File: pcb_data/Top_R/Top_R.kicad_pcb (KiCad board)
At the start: 2 copper layers, 186.9 x 96.4 mm, 93 parts, among them U1 XIAO-nRF52840

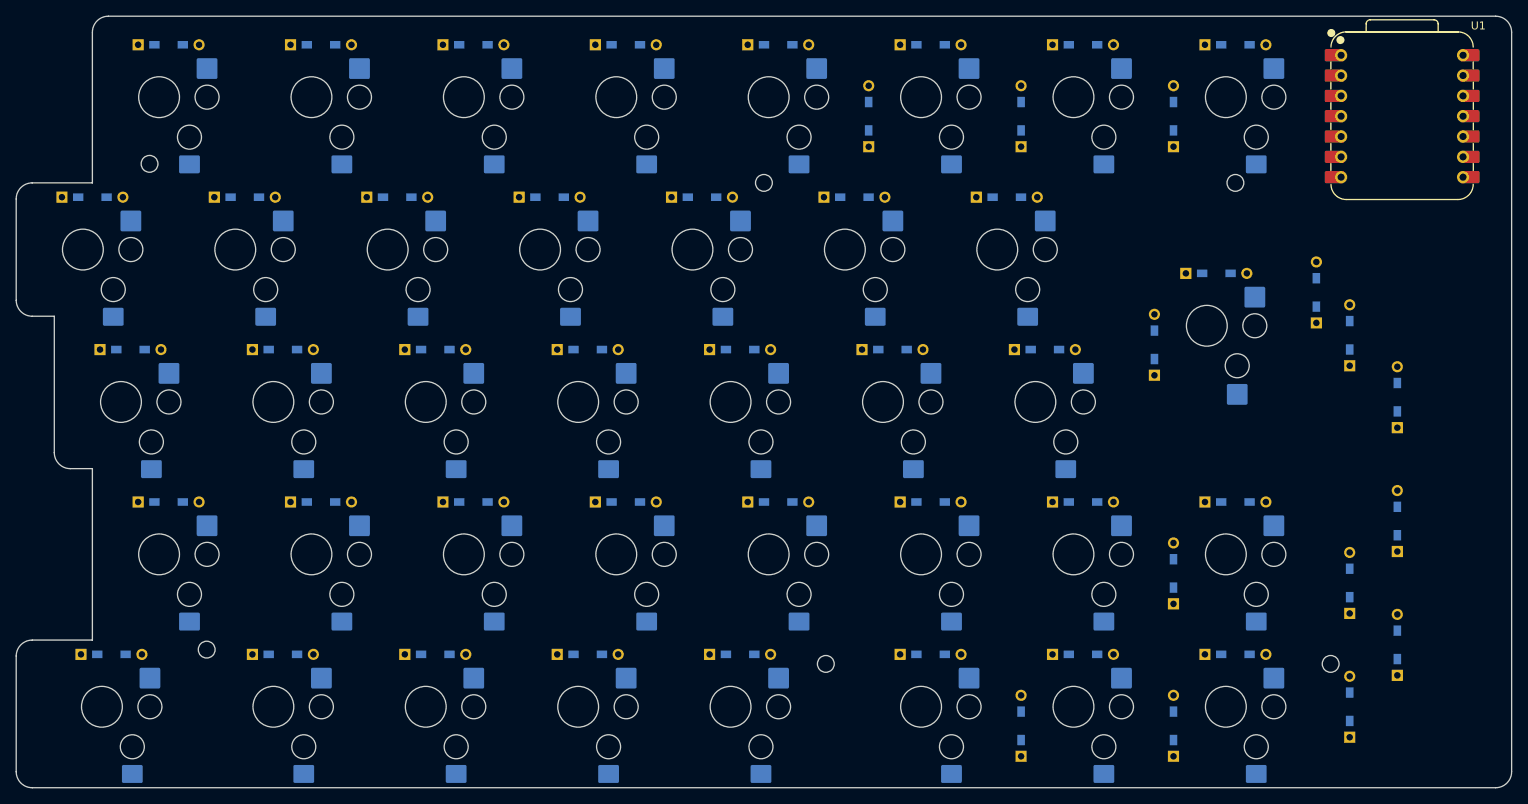
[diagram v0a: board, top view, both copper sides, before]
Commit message: remove diode
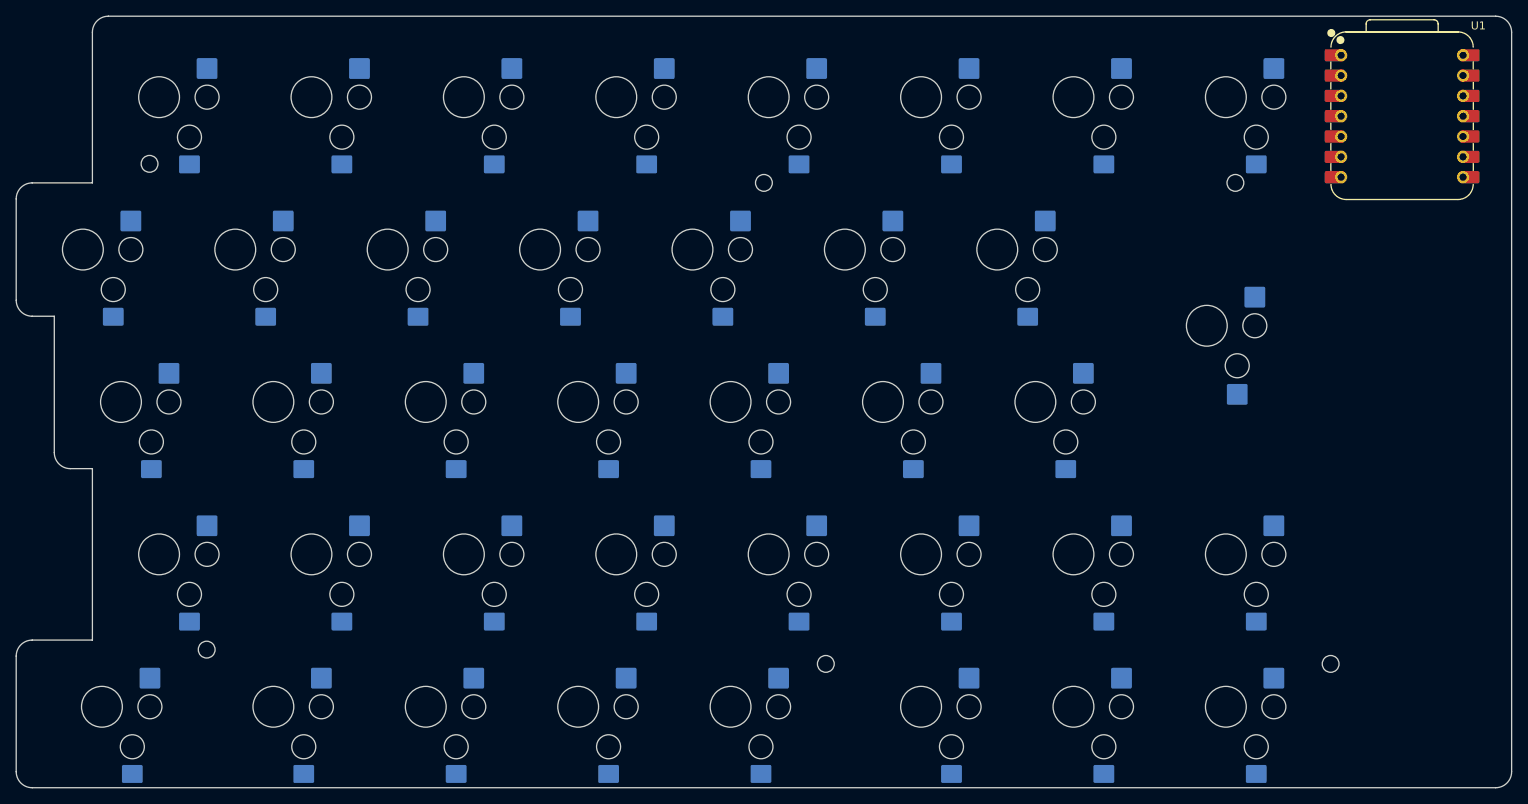
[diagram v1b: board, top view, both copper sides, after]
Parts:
- removed D0-10, D0-11, D0-12, D0-13, D0-8, D0-9, D1-10, D1-11, D1-12, D1-7, D1-9, D2-10, D2-11, D2-12, D2-13, D2-7, D2-8, D3-11, D3-12, D3-13, D3-7, D3-8, D3-9, D4-10, D4-12, D4-7, D4-8, D4-9, D5-10, D5-11, D5-13, D5-7, D5-8, D5-9, D6-10, D6-11, D6-12, D6-8, D6-9, DI10, DI11, DI12, DI13, DI7, DI8, DI9, DS10, DS11, DS12, DS13, DS7, DS8, DS9: 1N4148W, kbd_Parts:Diode_TH_SMD

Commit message: replace fp
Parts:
- RC0-13: footprint custom-library:Kailh-PG1353-Hotswap-R-1.25U -> kbd_SW_Hole:SW_Hole_1.25u
- RC6-10: footprint custom-library:Kailh-PG1353-Hotswap-ISOEnter-R -> kbd_SW_Hole:SW_Hole_2u
- turned RC6-10 to -90 degrees

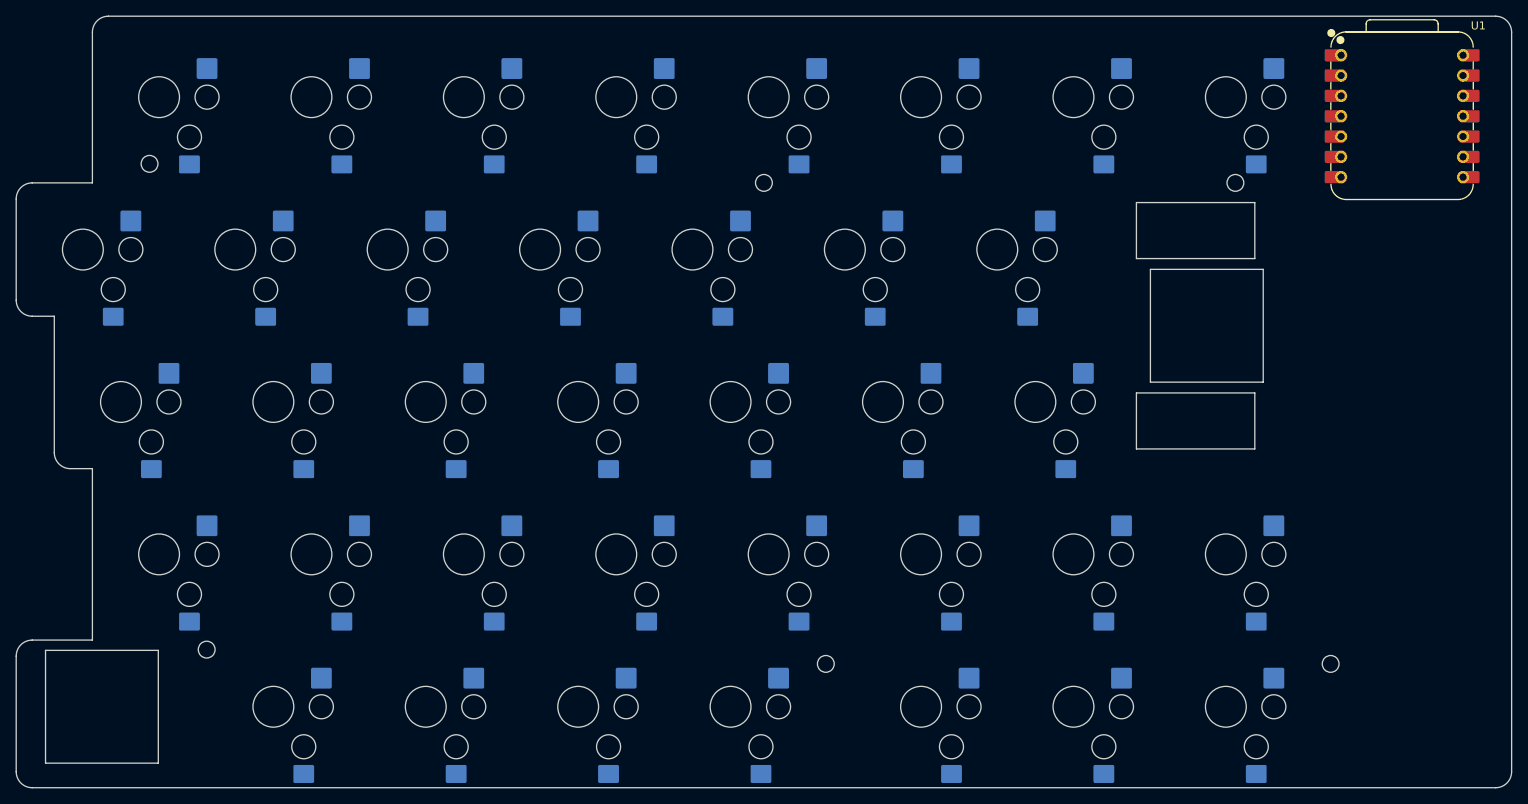
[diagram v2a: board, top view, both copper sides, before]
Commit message: replace fp
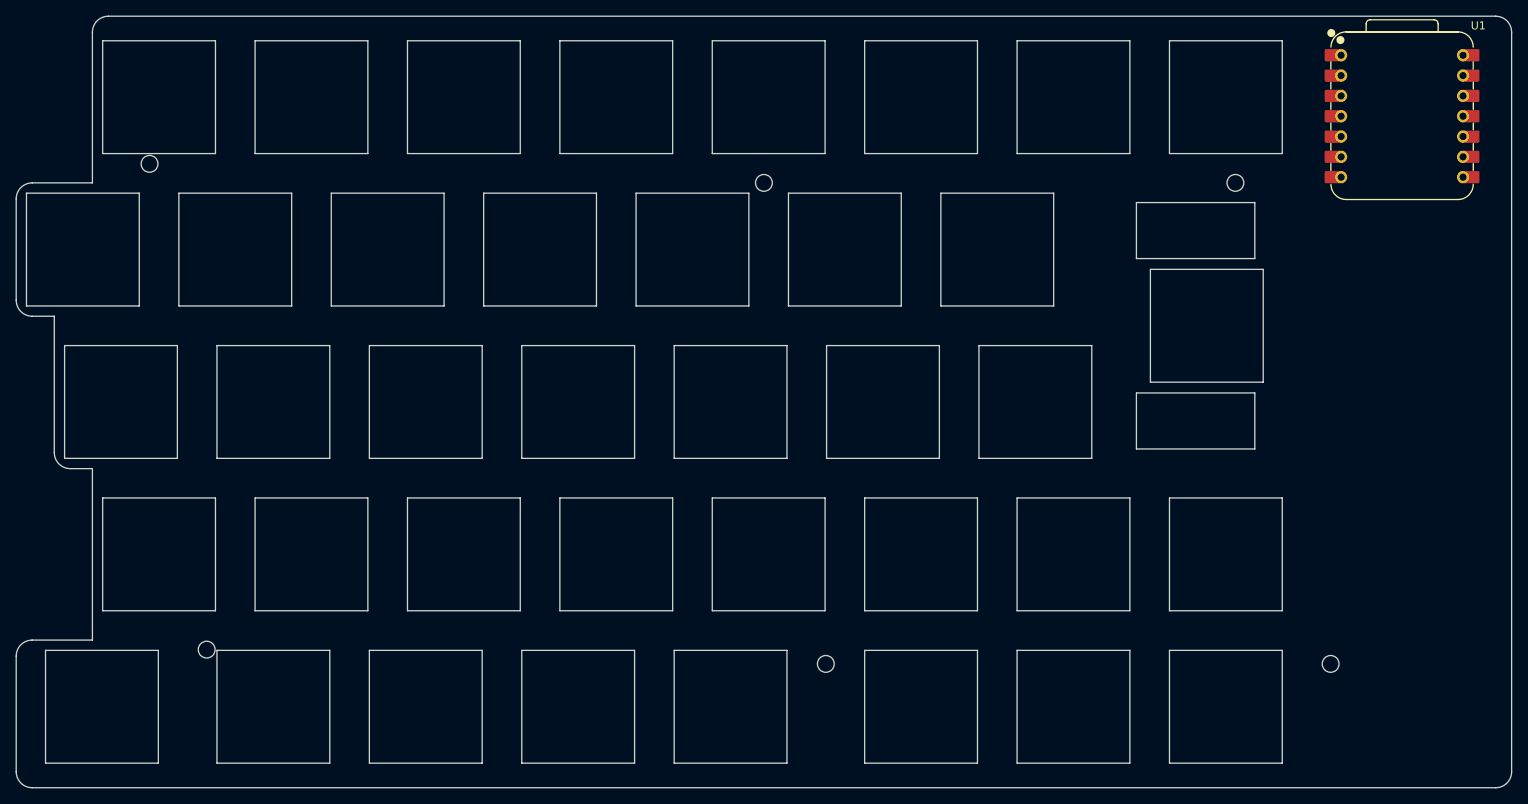
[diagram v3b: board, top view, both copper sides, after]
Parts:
- RC0-10, RC0-11, RC0-12, RC0-8, RC0-9, RC1-10, RC1-11, RC1-12, RC1-7, RC1-9, RC2-10, RC2-11, RC2-12, RC2-13, RC2-7, RC2-8, RC3-11, RC3-12, RC3-13, RC3-7, RC3-8, RC3-9, RC4-10, RC4-12, RC4-7, RC4-8, RC4-9, RC5-10, RC5-11, RC5-13, RC5-7, RC5-8, RC5-9, RC6-11, RC6-12, RC6-8, RC6-9: footprint custom-library:Kailh-PG1353-Hotswap-R-1U -> kbd_SW_Hole:SW_Hole_1u

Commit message: replace fp (m2 screw hole)
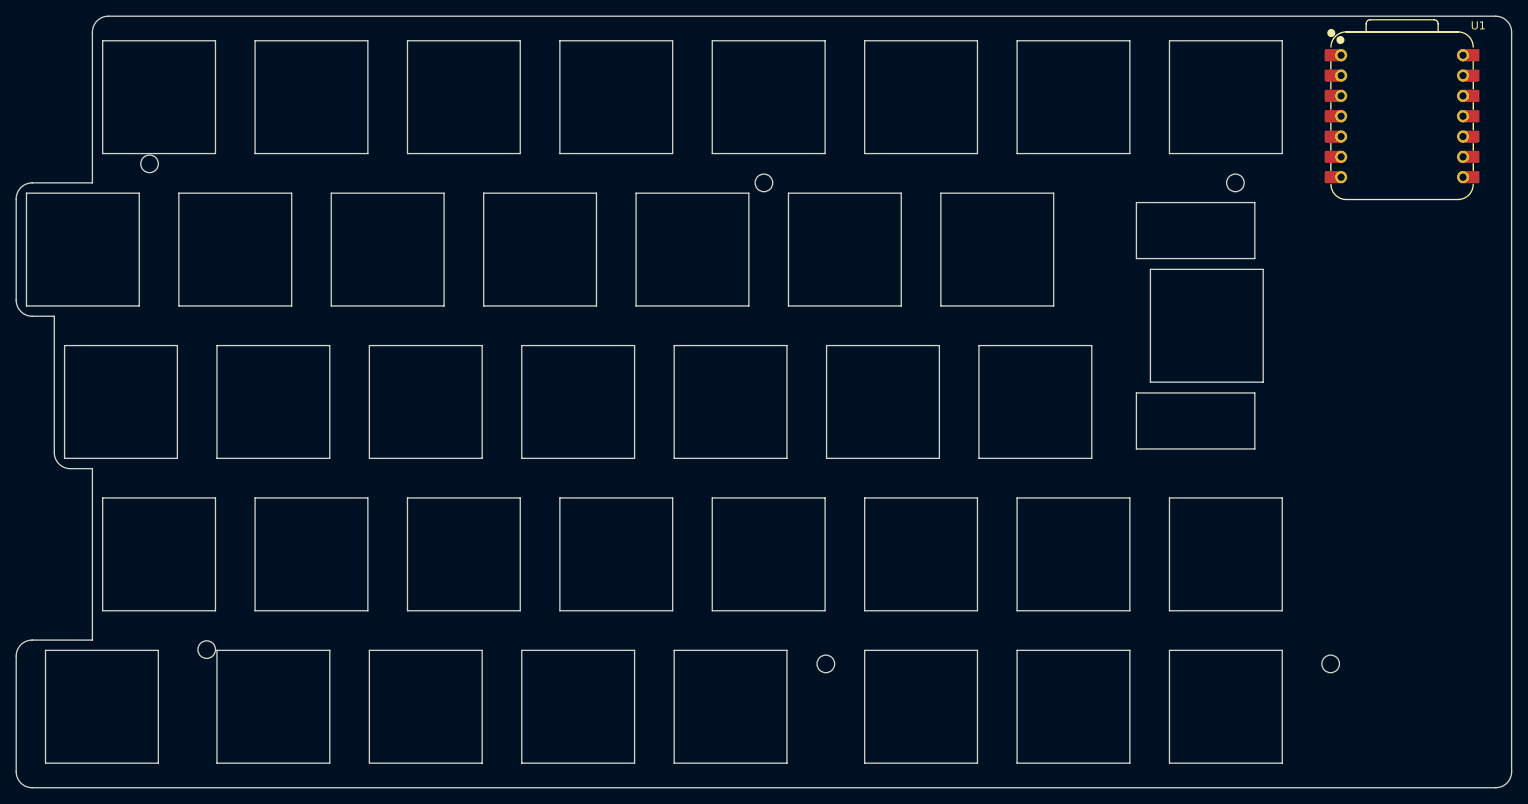
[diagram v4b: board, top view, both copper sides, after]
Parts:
- added Ref**: Val**, kbd_Hole:m2_Screw_Hole, F.Cu at (229.8, 128.0)
- added Ref**: Val**, kbd_Hole:m2_Screw_Hole, F.Cu at (89.3, 126.2)
- added Ref**: Val**, kbd_Hole:m2_Screw_Hole, F.Cu at (217.9, 67.9)
- added Ref**: Val**, kbd_Hole:m2_Screw_Hole, F.Cu at (82.2, 65.5)
- added Ref**: Val**, kbd_Hole:m2_Screw_Hole, F.Cu at (166.7, 128.0)
- added Ref**: Val**, kbd_Hole:m2_Screw_Hole, F.Cu at (158.9, 67.9)
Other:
- outline, holes or cut-outs redrawn
